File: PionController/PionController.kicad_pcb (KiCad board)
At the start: 4 copper layers, 82 x 60 mm, 84 parts, among them J1 SM10B-ULHK-1TA1-ETB_HF_, J2 Conn_01x02, J3 Conn_01x02, J4 Conn_01x02, J6 Conn_01x02, J7 FTSH-107-01-L-DV-K-A, U1 STM32H743VITx, U2 TLV75733PDBV, U3 ISO1050DUB, U4 ISO1050DUB, U5 CA-IS3740HN, X1 ASE-16.00MHz, Y2 32.768kHZ

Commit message: Before Library Fix (in case it goes wrong)
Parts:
- moved R13 10.2 mm to (124.2, 82.1)
- moved J7 2.76 mm to (129.8, 79.6), turned to -90 degrees
- moved C34 1.11 mm to (167.6, 78.7), turned to -90 degrees
- moved C33 0.89 mm to (162.6, 78.7), turned to 90 degrees
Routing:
- net Net-(J7-Pad13): track 49.3 -> 35.1 mm, vias 0 -> 2
- net Net-(J7-Pad14): track 16.3 -> 25.1 mm
- net Net-(J7-Pad12): track 9.69 -> 16.7 mm
- net Net-(J7-Pad04): track 24.9 -> 22.8 mm
- net GND: track 103.6 -> 101.8 mm, vias 67 -> 68
- net Net-(J7-Pad08): track 10.9 -> 12.6 mm
- net +3.3V: track 39.9 -> 41.3 mm, vias 16 -> 15
- net Net-(U3-CANH): track 14.1 -> 15.0 mm
- net Net-(U3-CANL): track 15.0 -> 15.6 mm
- added copper zone on F.Cu, net GND

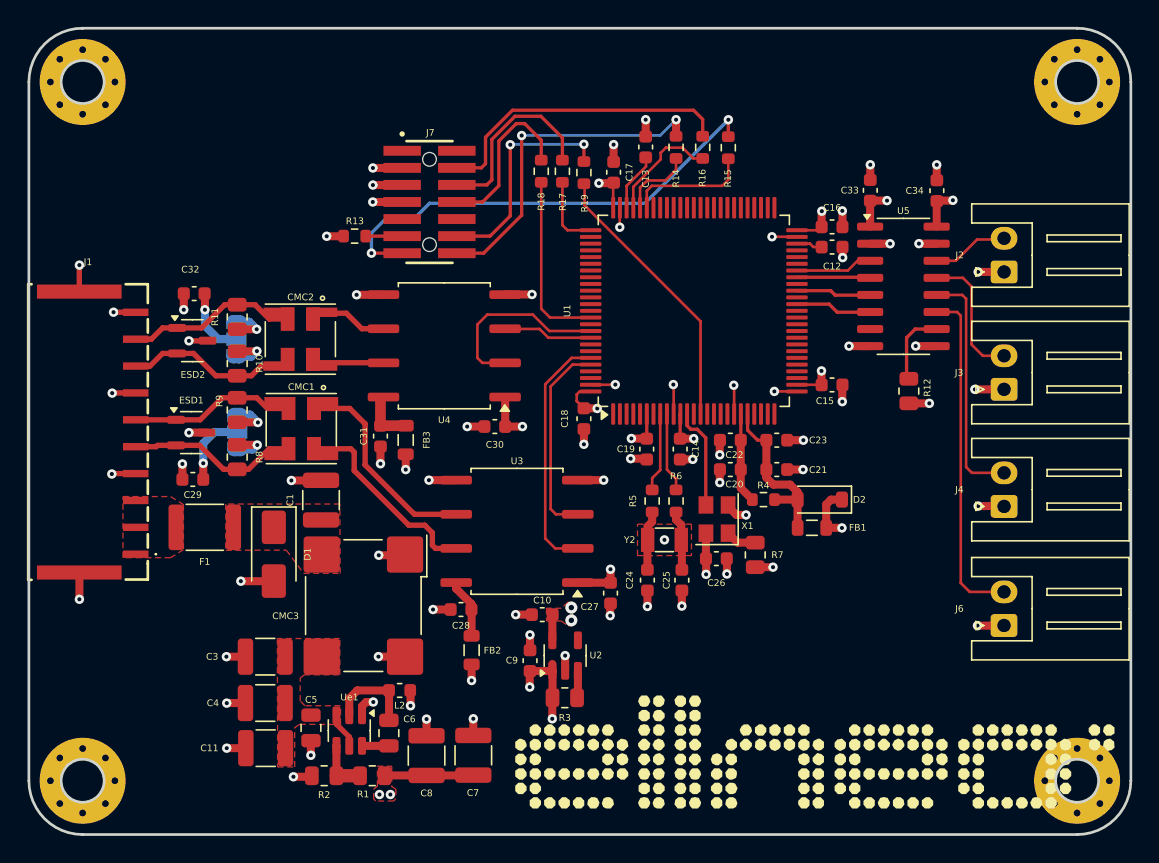
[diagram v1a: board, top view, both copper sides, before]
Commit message: Librery fix, 3d models added and fiducial marks
Library Fix: Added missing components and updated footprints, ensuring all parts are properly referenced.
3D Models Added: Integrated 3D models for visual reference in the PCB layout and to assist with mechanical fitment checks.
Fiducial Marks: Placed fiducial marks on the board for accurate alignment during automated assembly processes.
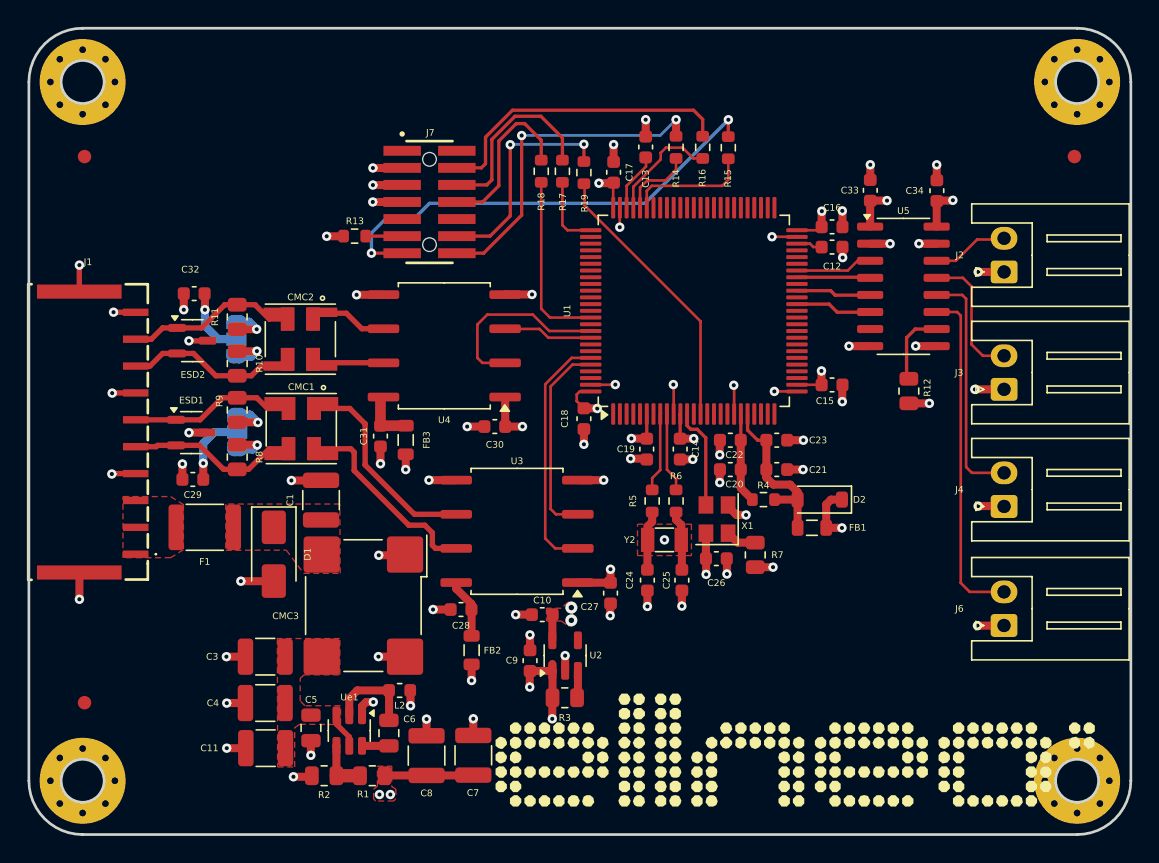
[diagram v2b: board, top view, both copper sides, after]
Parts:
- added FID2: Fiducial, Fiducial:Fiducial_1mm_Mask2mm, F.Cu at (177.8, 76.2)
- added FID2: Fiducial, Fiducial:Fiducial_1mm_Mask2mm, F.Cu at (104.1, 116.8)
- added FID2: Fiducial, Fiducial:Fiducial_1mm_Mask2mm, F.Cu at (104.1, 76.2)

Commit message: Fixed mispositioned elements, made power and ground connections thicker, and cleared the power plane gap from vias.
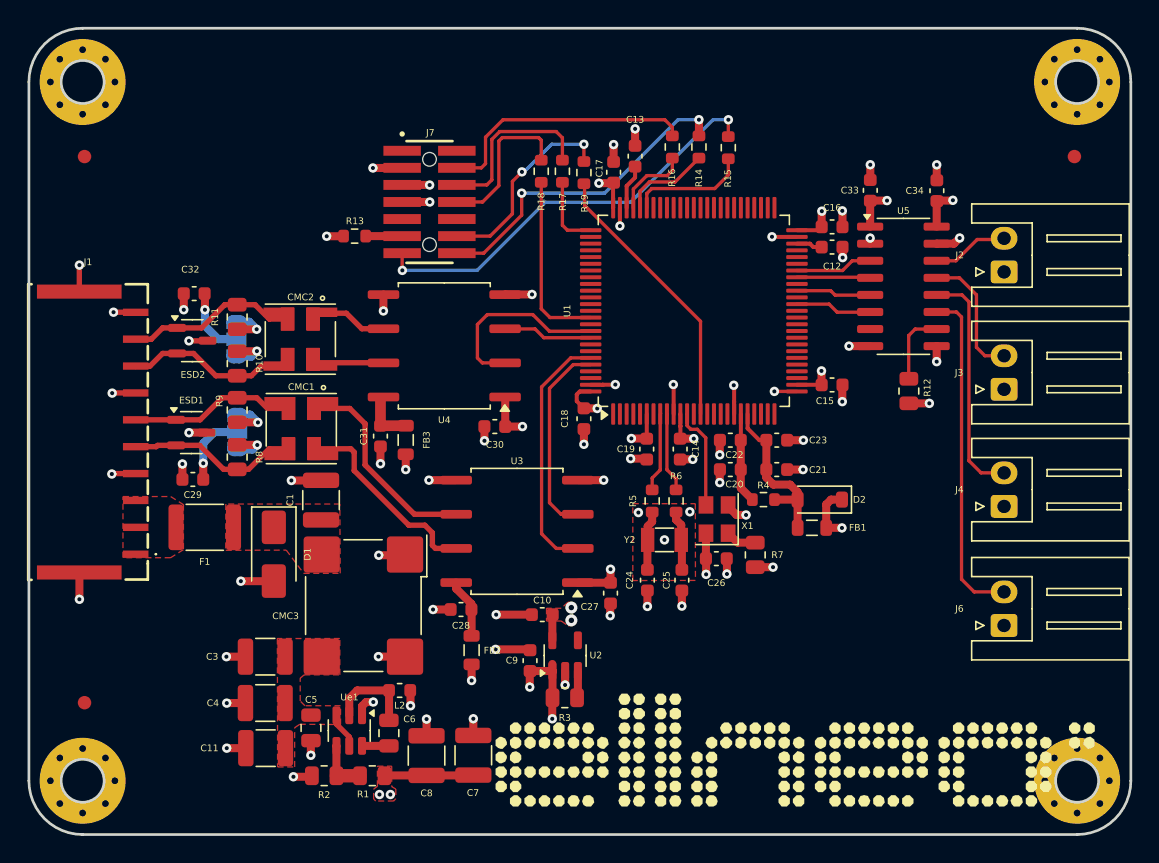
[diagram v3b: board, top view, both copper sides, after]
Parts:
- moved R16 2.26 mm to (147.9, 75.5)
- moved R14 1.70 mm to (149.9, 75.5)
- moved C13 1.04 mm to (145.1, 76.2)
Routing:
- net GND: track 101.8 -> 94.4 mm, vias 68 -> 66
- net Net-(J7-Pad13): track 35.1 -> 31.4 mm
- net Net-(J7-Pad04): track 22.8 -> 19.5 mm
- net SWDIO: track 8.54 -> 5.78 mm
- net Net-(J7-Pad12): track 16.7 -> 15.0 mm
- net Net-(C13-Pad2): track 4.42 -> 3.32 mm
- net UART4_TX: track 5.57 -> 6.63 mm
- net Net-(J7-Pad06): track 14.1 -> 13.1 mm
- net Net-(J7-Pad08): track 12.6 -> 11.8 mm
- net Net-(J7-Pad14): track 25.1 -> 24.3 mm

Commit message: fixing logo scale
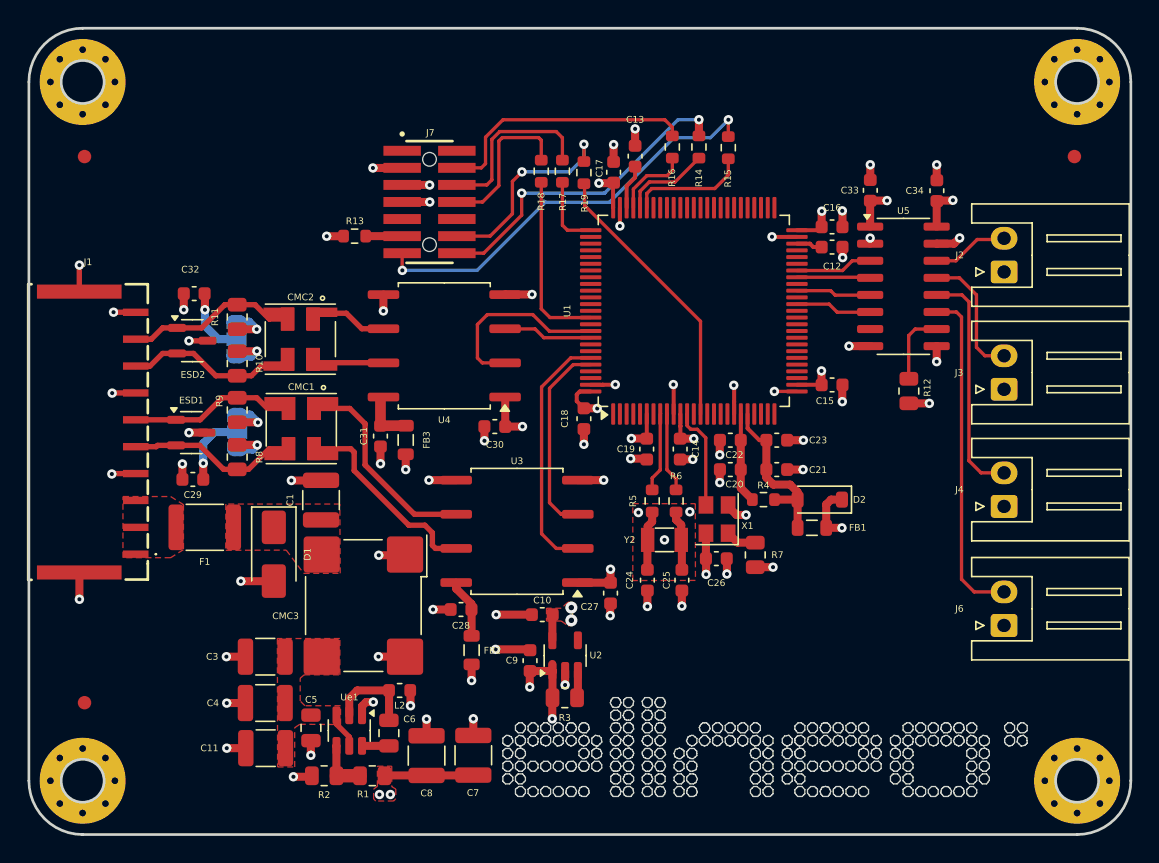
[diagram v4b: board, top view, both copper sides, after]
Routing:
- net Net-(J7-Pad12): track 15.0 -> 15.6 mm
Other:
- outline, holes or cut-outs redrawn
